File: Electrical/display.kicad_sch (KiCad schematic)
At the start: 4 parts, among them U6 DA56-11CGKWA

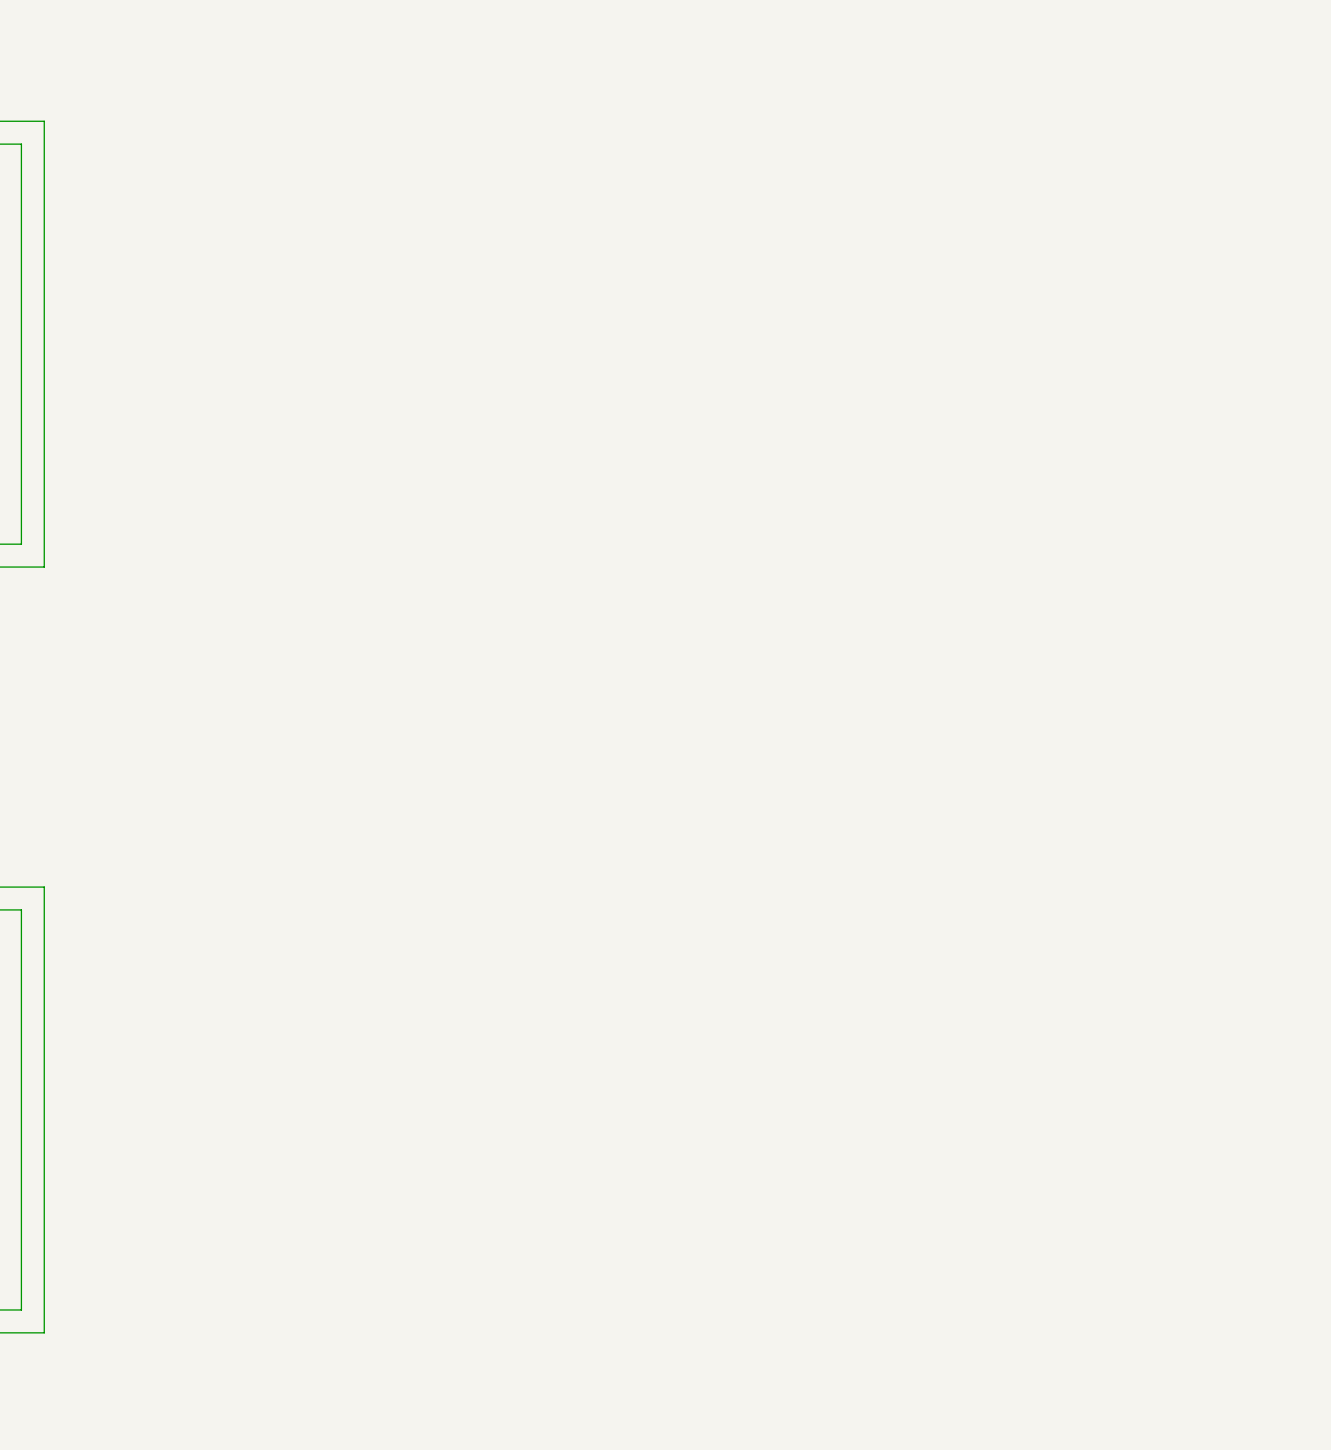
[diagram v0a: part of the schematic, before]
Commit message: Added Alphanumeric display
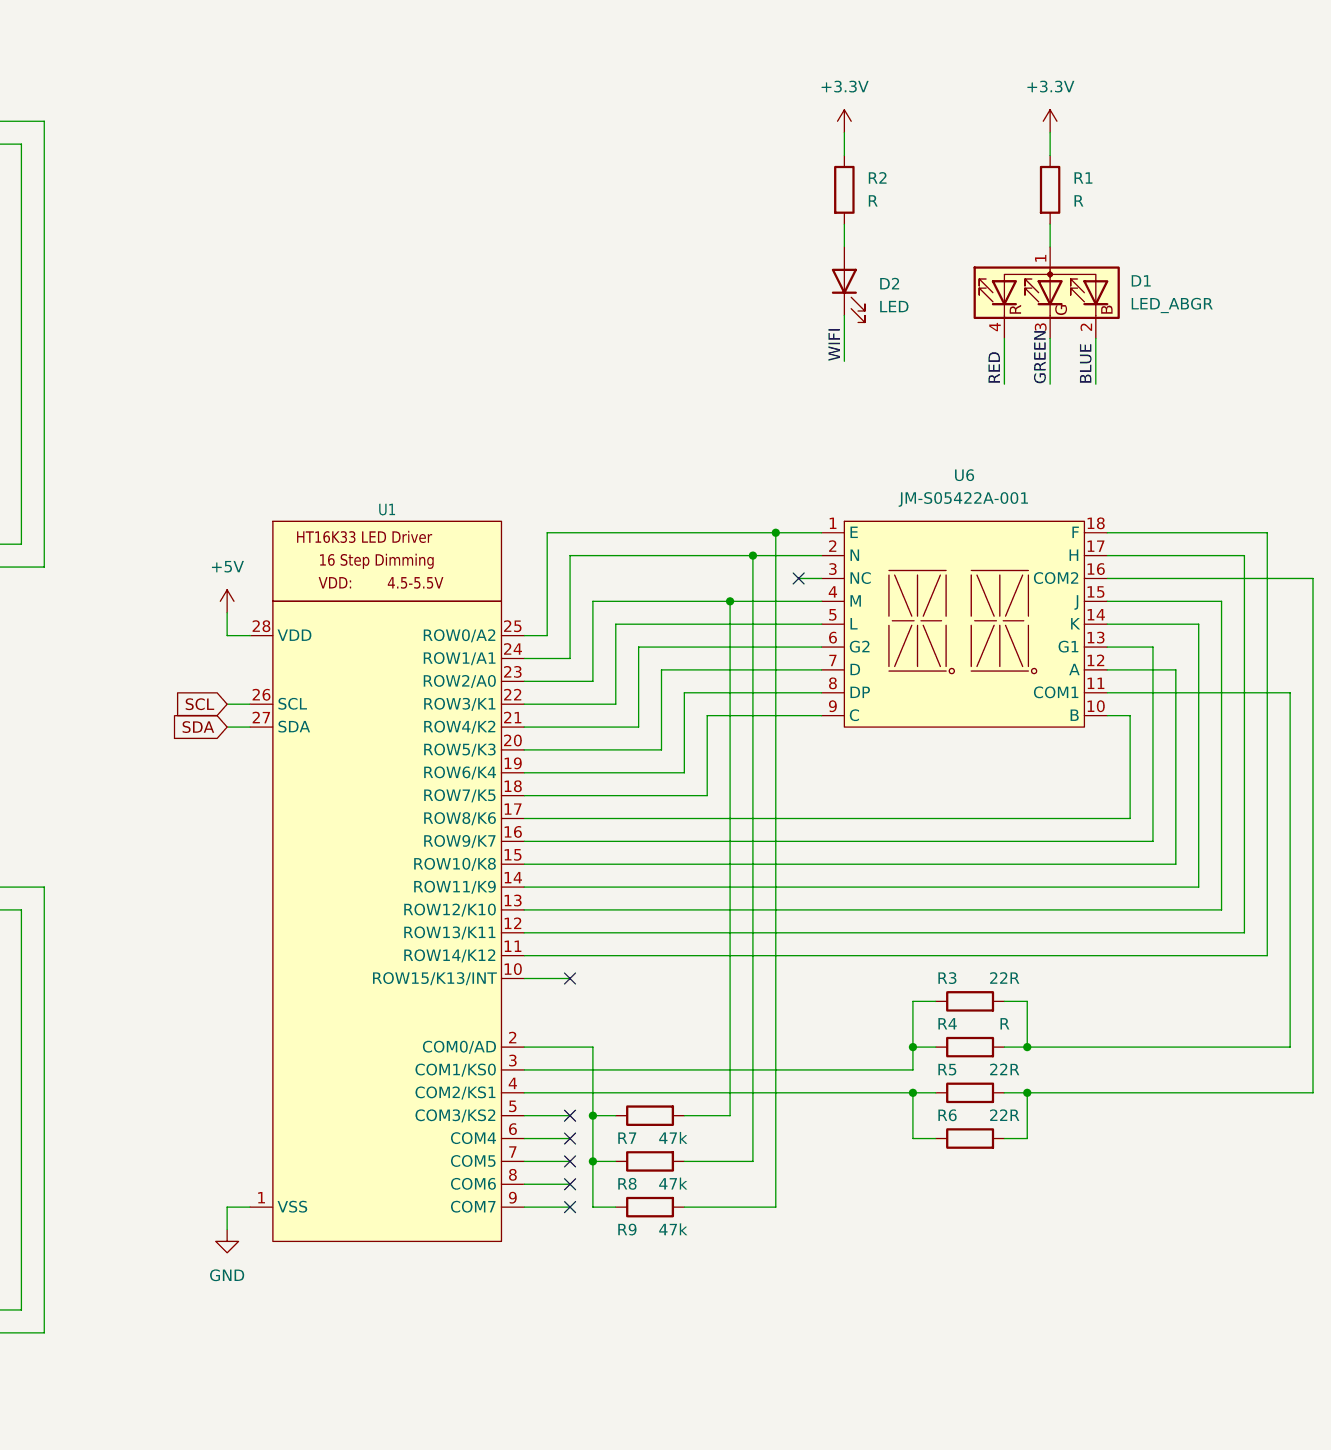
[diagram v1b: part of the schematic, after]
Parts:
- added D1: LED_ABGR, symbol Device:LED_ABGR
- added D2: LED, symbol Device:LED
- added R1, R2, R4: R, symbol Device:R
- added R3, R5, R6: 22R, symbol Device:R
- added R7, R8, R9: 47k, symbol Device:R
- added U1: ~, Adafruit 0.56 7-Segment QT:SOP28_300MIL, symbol Adafruit 0.56 7-Segment QT-eagle-import:HT16K33_SOP28
- added U6: JM-S05422A-001, symbol Display_Character:JM-S05422AH-001
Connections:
- net +5V: now also U1.28 (VDD)
- net GND: now also U1.1 (VSS)
- net SCL: now also U1.26 (SCL)
- net SDA: now also U1.27 (SDA)
- new net: U1.11 (ROW14/K12), U6.18 (F)
- new net: U1.12 (ROW13/K11), U6.17 (H)
- new net: U1.13 (ROW12/K10), U6.15 (J)
- new net: U1.14 (ROW11/K9), U6.14 (K)
- new net: U1.15 (ROW10/K8), U6.12 (A)
- new net: U1.16 (ROW9/K7), U6.13 (G1)
- new net: U1.17 (ROW8/K6), U6.10 (B)
- new net: U1.18 (ROW7/K5), U6.9 (C)
- new net: U1.19 (ROW6/K4), U6.8 (DP)
- new net: R7.1, R8.1, R9.1, U1.2 (COM0/AD)
- new net: U1.20 (ROW5/K3), U6.7 (D)
- new net: U1.21 (ROW4/K2), U6.6 (G2)
- new net: U1.22 (ROW3/K1), U6.5 (L)
- new net: R7.2, U1.23 (ROW2/A0), U6.4 (M)
- new net: R8.2, U1.24 (ROW1/A1), U6.2 (N)
- new net: R9.2, U1.25 (ROW0/A2), U6.1 (E)
- new net: R3.1, R4.1, U1.3 (COM1/KS0)
- new net: R5.1, R6.1, U1.4 (COM2/KS1)
- new net: R5.2, R6.2, U6.16 (COM2)
- new net: D1.1 (A), R1.2
- new net: R3.2, R4.2, U6.11 (COM1)
- new net: D2.2 (A), R2.2
- new net +3.3V: R1.1, R2.1
- new net BLUE: D1.2 (BK)
- new net GREEN: D1.3 (GK)
- new net RED: D1.4 (RK)
- new net WIFI: D2.1 (K)
- no-connect marks 0 -> 7

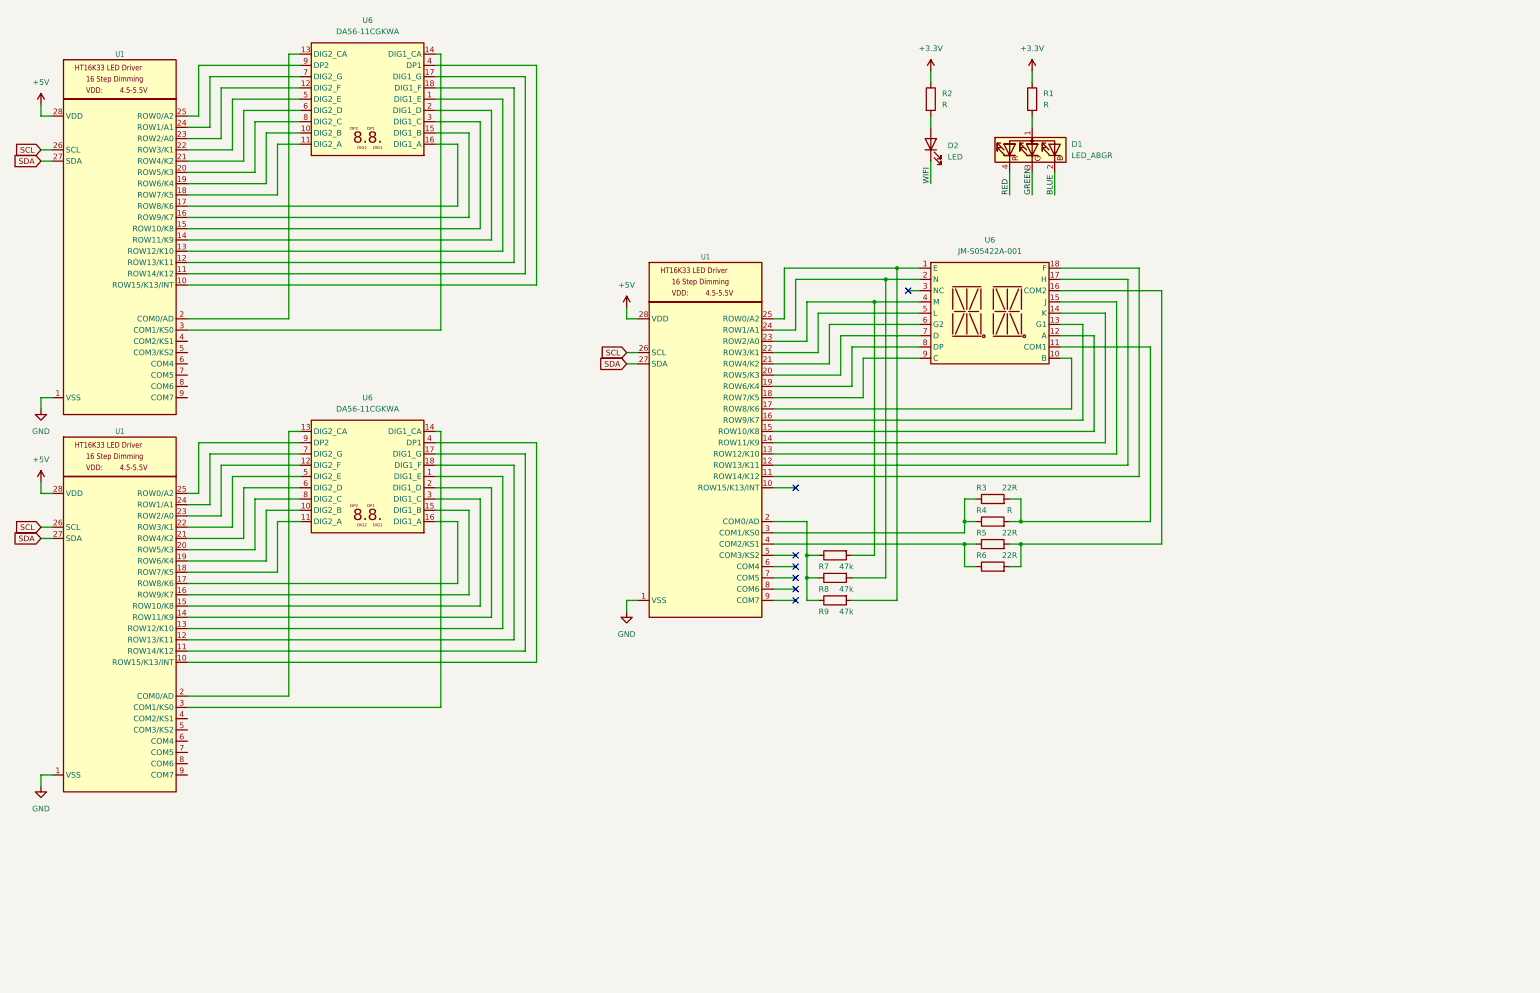
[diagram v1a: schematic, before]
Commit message: Added I2C adresses
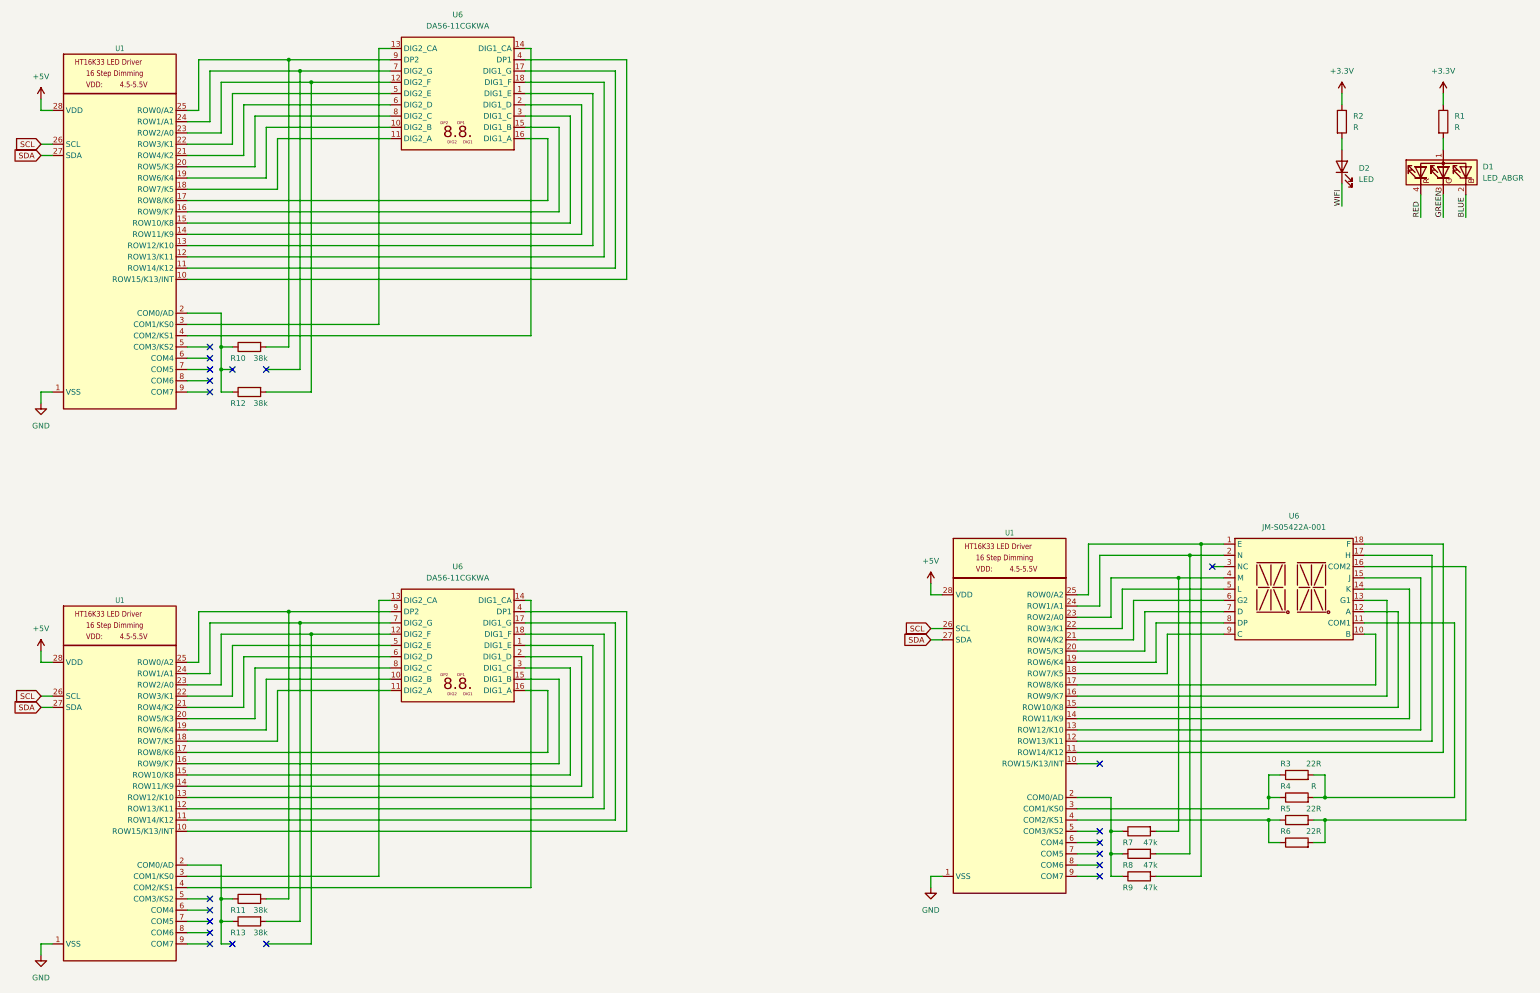
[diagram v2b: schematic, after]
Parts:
- added R10, R11, R12, R13: 38k, symbol Device:R
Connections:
- net at U1.2 (COM0/AD): now also R11.1, R13.1; no longer U6.13 (DIG2_CA)
- net at U1.24 (ROW1/A1), U6.7 (DIG2_G): now also R13.2
- net at U1.25 (ROW0/A2), U6.9 (DP2): now also R11.2
- net at U1.3 (COM1/KS0): now also U6.13 (DIG2_CA); no longer U6.14 (DIG1_CA) (x2)
- net at U1.4 (COM2/KS1): now also U6.14 (DIG1_CA) (x2)
- net at U1.23 (ROW2/A0), U6.12 (DIG2_F): now also R12.2
- net at U1.2 (COM0/AD): now also R10.1, R12.1; no longer U6.13 (DIG2_CA)
- net at U1.25 (ROW0/A2), U6.9 (DP2): now also R10.2
- no-connect marks 7 -> 21
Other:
- moved on the sheet: D1, D2, R1, R2, R3, R4, R5, R6, R7, R8, R9, U1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

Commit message: Added Display PCB
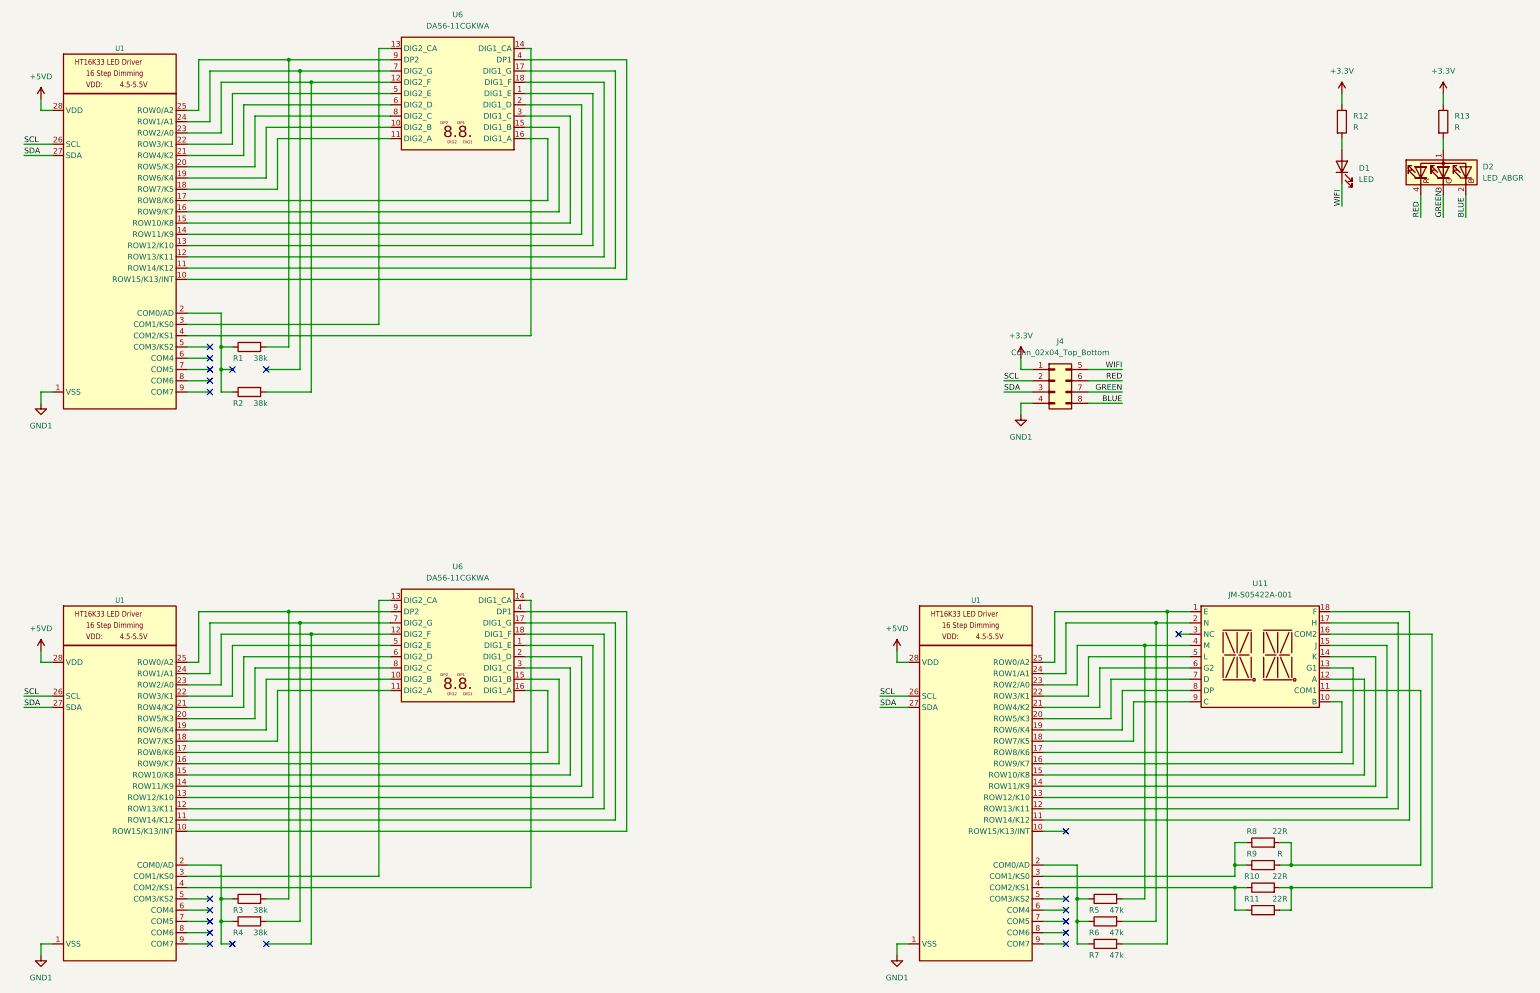
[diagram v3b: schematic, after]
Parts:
- added J4: Conn_02x04_Top_Bottom, Connector_IDC:IDC-Header_2x04_P2.54mm_Vertical, symbol Connector_Generic:Conn_02x04_Top_Bottom
- D1: renamed from D2; footprint (none) -> LED_THT:LED_D5.0mm
- D2: renamed from D1; footprint (none) -> LED_THT:LED_D5.0mm-4_RGB_Wide_Pins
- R1: renamed from R10; footprint (none) -> Resistor_THT:R_Axial_DIN0204_L3.6mm_D1.6mm_P5.08mm_Horizontal
- R10: renamed from R5; footprint (none) -> Resistor_THT:R_Axial_DIN0204_L3.6mm_D1.6mm_P5.08mm_Horizontal
- R11: renamed from R6; footprint (none) -> Resistor_THT:R_Axial_DIN0204_L3.6mm_D1.6mm_P5.08mm_Horizontal
- R12: renamed from R2; footprint (none) -> Resistor_THT:R_Axial_DIN0204_L3.6mm_D1.6mm_P5.08mm_Horizontal
- R13: renamed from R1; footprint (none) -> Resistor_THT:R_Axial_DIN0204_L3.6mm_D1.6mm_P5.08mm_Horizontal
- R2: renamed from R12; footprint (none) -> Resistor_THT:R_Axial_DIN0204_L3.6mm_D1.6mm_P5.08mm_Horizontal
- R3: renamed from R11; footprint (none) -> Resistor_THT:R_Axial_DIN0204_L3.6mm_D1.6mm_P5.08mm_Horizontal
- R4: renamed from R13; footprint (none) -> Resistor_THT:R_Axial_DIN0204_L3.6mm_D1.6mm_P5.08mm_Horizontal
- R5: renamed from R7; footprint (none) -> Resistor_THT:R_Axial_DIN0204_L3.6mm_D1.6mm_P5.08mm_Horizontal
- R6: renamed from R8; footprint (none) -> Resistor_THT:R_Axial_DIN0204_L3.6mm_D1.6mm_P5.08mm_Horizontal
- R7: renamed from R9; footprint (none) -> Resistor_THT:R_Axial_DIN0204_L3.6mm_D1.6mm_P5.08mm_Horizontal
- R8: renamed from R3; footprint (none) -> Resistor_THT:R_Axial_DIN0204_L3.6mm_D1.6mm_P5.08mm_Horizontal
- R9: renamed from R4; footprint (none) -> Resistor_THT:R_Axial_DIN0204_L3.6mm_D1.6mm_P5.08mm_Horizontal
- U1: footprint Adafruit 0.56 7-Segment QT:SOP28_300MIL -> Package_SO:SSOP-28_3.9x9.9mm_P0.635mm
- U11: renamed from U6; footprint (none) -> Display_7Segment:DA56-11CGKWA
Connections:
- net +3.3V: now also J4.1 (Pin_1)
- net BLUE: now also J4.8 (Pin_8)
- net GREEN: now also J4.7 (Pin_7)
- net RED: now also J4.6 (Pin_6)
- net SCL: now also J4.2 (Pin_2)
- net SDA: now also J4.3 (Pin_3)
- net WIFI: now also J4.5 (Pin_5)
- net +5V renamed +5VD
- net GND renamed GND1
- net GND1: now also J4.4 (Pin_4)
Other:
- moved on the sheet: R10, R11, R5, R6, R7, R8, R9, U1, U11
